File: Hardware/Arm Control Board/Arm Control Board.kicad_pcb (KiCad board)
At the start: 2 copper layers, 112 parts, among them P1 Servo 1, P10 UIM240XX_Stepper_Conn, P11 Battery, P12 SyRen, P13 Raspberry Pi, P14 Gripper Force Fdbk, P2 Shoulder Feedback, P3 Servo 2, P4 Servo 3, P5 Elbow Feedback, P6 Servo 4, P7 RS485, P8 ST_SWD_Connector, P9 Servo 5, U1 STM32F401RCT6, U10 ZXCT1107, U11 ZXCT1107, U12 ZXCT1107, U13 ZXCT1107, U2 SN75176BDR, U3 74LVCH244APW, U4 AOZ1280CI, U5 AOZ1280CI, U6 AP65552SP-13, U7 AP65552SP-13, U8 AP65552SP-13, U9 AP65552SP-13, X1 24MHz

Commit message: Connecting more things in better ways
Just in case i screw something up
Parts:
- moved P13 130.7 mm to (161.2, 101.8), turned to 0 degrees
- moved P7 127.0 mm to (185.8, 114.2), turned to 0 degrees
- moved U2 121.4 mm to (192.4, 114.2)
- moved P12 116.0 mm to (195.2, 100.4), turned to 90 degrees
- moved C1 112.9 mm to (192.2, 110.0)
- moved C51 106.9 mm to (215.4, 100.6)
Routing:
- net /Servo1_PWM: track 0.00 -> 113.4 mm, vias 0 -> 6
- net /7.4V Regulators/REG1EN: track 0.01 -> 107.4 mm, vias 0 -> 4
- net /7.4V Regulators/REG4CURRENT: track 4.01 -> 85.2 mm, vias 0 -> 4
- net /7.4V Regulators/REG1CURRENT: track 3.27 -> 77.3 mm
- net /Servo5_PWM: track 0.00 -> 68.6 mm, vias 0 -> 2
- net /Low Voltage Regulators/REG5+5V: track 0.00 -> 62.5 mm, vias 0 -> 4
- net /Low Voltage Regulators/REG5EN: track 0.22 -> 61.1 mm, vias 0 -> 4
- net /7.4V Regulators/REG4EN: track 0.99 -> 55.5 mm, vias 0 -> 2
- net /Servo4_PWM: track 0.00 -> 50.1 mm, vias 0 -> 2
- net /Servo3_PWM: track 0.00 -> 25.0 mm
- net /USART1_RX: track 0.00 -> 17.8 mm, vias 0 -> 2
- net Net-(C51-Pad1): track 1.13 -> 14.1 mm, vias 0 -> 2
- net /USART1_TX: track 0.00 -> 12.6 mm
- net Net-(U1-Pad41): track 1.27 -> 13.2 mm
- net /485_B: track 11.5 -> 3.08 mm
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
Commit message: Connect everything but 12V and GND
Not like those lines are really necessary. MAVRIC is more than capable
of running off of team spirit, optimism, and enthusiasm.
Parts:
- moved P11 142.5 mm to (156.0, 116.0), turned to 90 degrees
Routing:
- net /7.4V Regulators/REG3CURRENT: track 2.77 -> 177.2 mm, vias 0 -> 8
- net /7.4V Regulators/REG2EN: track 0.00 -> 130.2 mm, vias 0 -> 4
- net /7.4V Regulators/REG2CURRENT: track 3.08 -> 105.8 mm, vias 0 -> 2
- net /Low Voltage Regulators/REG6EN: track 0.47 -> 99.1 mm, vias 0 -> 2
- net /Servo2_PWM: track 0.00 -> 96.5 mm, vias 0 -> 4
- net /ADC1_IN9_Elbow: track 0.00 -> 95.0 mm, vias 0 -> 4
- net /ADC1_IN8_Shoulder: track 0.21 -> 89.9 mm, vias 0 -> 4
- net /ADC1_IN10_GripForce: track 0.00 -> 63.5 mm, vias 0 -> 4
- net /7.4V Regulators/REG3EN: track 0.49 -> 55.5 mm, vias 0 -> 8
- net /Low Voltage Regulators/REG6+3V3: track 91.7 -> 145.2 mm, vias 0 -> 4
- net /Step_Step: track 0.00 -> 21.7 mm, vias 0 -> 2
- net /Low Voltage Regulators/REG5+5V: track 62.5 -> 75.7 mm
- net /Low Voltage Regulators/REG5EN: track 61.1 -> 72.0 mm
- net /Step_Enable: track 20.2 -> 18.5 mm
- net /Servo1_PWM: track 113.4 -> 114.7 mm
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
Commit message: Condensing Stage 1
Just an intermediate commit in case something goes horribly wrong
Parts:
- moved C35 16.3 mm to (221.2, 143.8)
- moved C37 16.3 mm to (226.2, 143.0)
- moved C39 16.3 mm to (231.2, 140.8)
- moved C41 16.3 mm to (230.4, 135.5)
- moved C43 16.3 mm to (220.9, 135.0)
- moved C44 16.3 mm to (233.2, 135.5)
- moved C47 16.3 mm to (224.4, 127.5)
- moved C49 16.3 mm to (218.2, 135.0)
- moved L5 16.3 mm to (230.2, 127.5)
- moved P4 16.3 mm to (229.3, 115.2)
- moved R11 16.3 mm to (221.2, 146.5)
- moved R13 16.3 mm to (221.2, 141.0)
- moved R15 16.3 mm to (215.4, 135.0)
- moved R21 16.3 mm to (229.3, 120.2)
- moved R23 16.3 mm to (235.1, 114.9)
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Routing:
- net /7.4V Regulators/REG3CURRENT: track 177.2 -> 130.0 mm, vias 8 -> 10
- net /Servo3_PWM: track 25.0 -> 8.26 mm
- net /Servo2_PWM: track 96.5 -> 85.5 mm
- net /Servo1_PWM: track 114.7 -> 104.6 mm
- net /7.4V Regulators/REG3EN: track 55.5 -> 46.3 mm
- net /ADC1_IN10_GripForce: track 63.5 -> 56.5 mm
- net /ADC1_IN8_Shoulder: track 89.9 -> 85.5 mm
- net /Servo4_PWM: track 50.9 -> 47.1 mm
- net Net-(C22-Pad1): track 0.00 -> 3.14 mm
- net /Low Voltage Regulators/REG6EN: track 99.1 -> 101.5 mm
- net /Low Voltage Regulators/REG6+3V3: track 145.2 -> 144.1 mm
- net /7.4V Regulators/REG2CURRENT: track 105.8 -> 106.4 mm

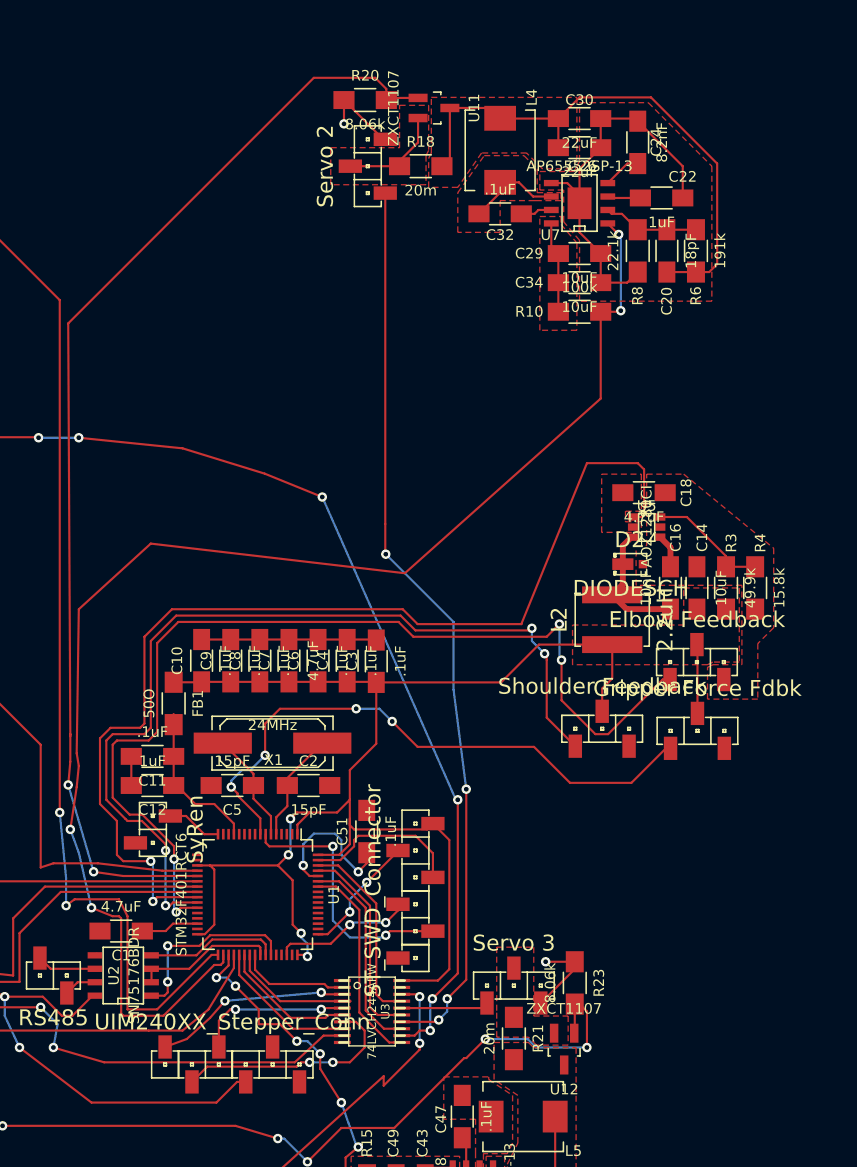
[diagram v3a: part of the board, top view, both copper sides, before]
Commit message: Condensing Stage 2
Still in progress, many of the traces are now in reasonable, space
conservative spots
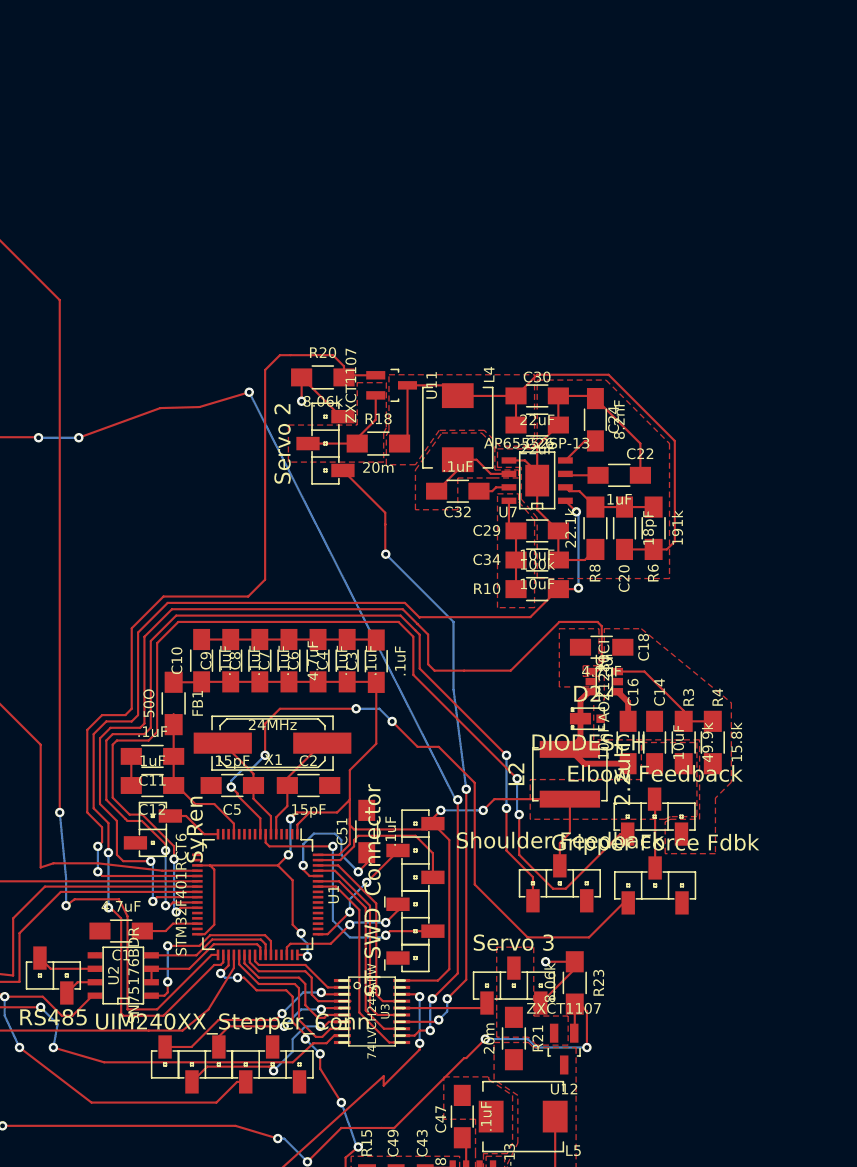
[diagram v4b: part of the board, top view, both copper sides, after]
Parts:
- moved C20 26.5 mm to (239.8, 72.0)
- moved C22 26.5 mm to (239.2, 67.0)
- moved C24 26.5 mm to (237.0, 61.7)
- moved C26 26.5 mm to (231.5, 62.2)
- moved C29 26.5 mm to (231.5, 72.2)
- moved C30 26.5 mm to (231.5, 59.5)
- moved C32 26.5 mm to (224.0, 68.5)
- moved C34 26.5 mm to (231.5, 75.0)
- moved L4 26.5 mm to (224.0, 62.5)
- moved P3 26.5 mm to (211.5, 64.0)
- moved R10 26.5 mm to (231.5, 77.7)
- moved R18 26.5 mm to (216.5, 64.0)
- moved R20 26.5 mm to (211.2, 57.7)
- moved R6 26.5 mm to (242.5, 72.0)
- moved R8 26.5 mm to (237.0, 72.0)
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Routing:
- net /Servo2_PWM: track 85.5 -> 61.0 mm
- net /7.4V Regulators/REG2EN: track 130.2 -> 106.1 mm
- net /7.4V Regulators/REG2CURRENT: track 106.4 -> 83.2 mm
- net /Low Voltage Regulators/REG6+3V3: track 144.1 -> 134.6 mm, vias 4 -> 6
- net /Low Voltage Regulators/REG6EN: track 101.5 -> 92.2 mm
- net /ADC1_IN10_GripForce: track 56.5 -> 64.2 mm
- net /ADC1_IN8_Shoulder: track 85.5 -> 91.7 mm
- net /Servo1_PWM: track 104.6 -> 109.5 mm
- net /Step_Step: track 21.7 -> 17.6 mm
- net /ADC1_IN9_Elbow: track 95.2 -> 98.3 mm
- net /TIM3_CH1_EE: track 13.8 -> 15.6 mm
- net /Step_Direction: track 14.6 -> 13.8 mm
- net /TIM3_CH2_EE: track 12.8 -> 13.5 mm

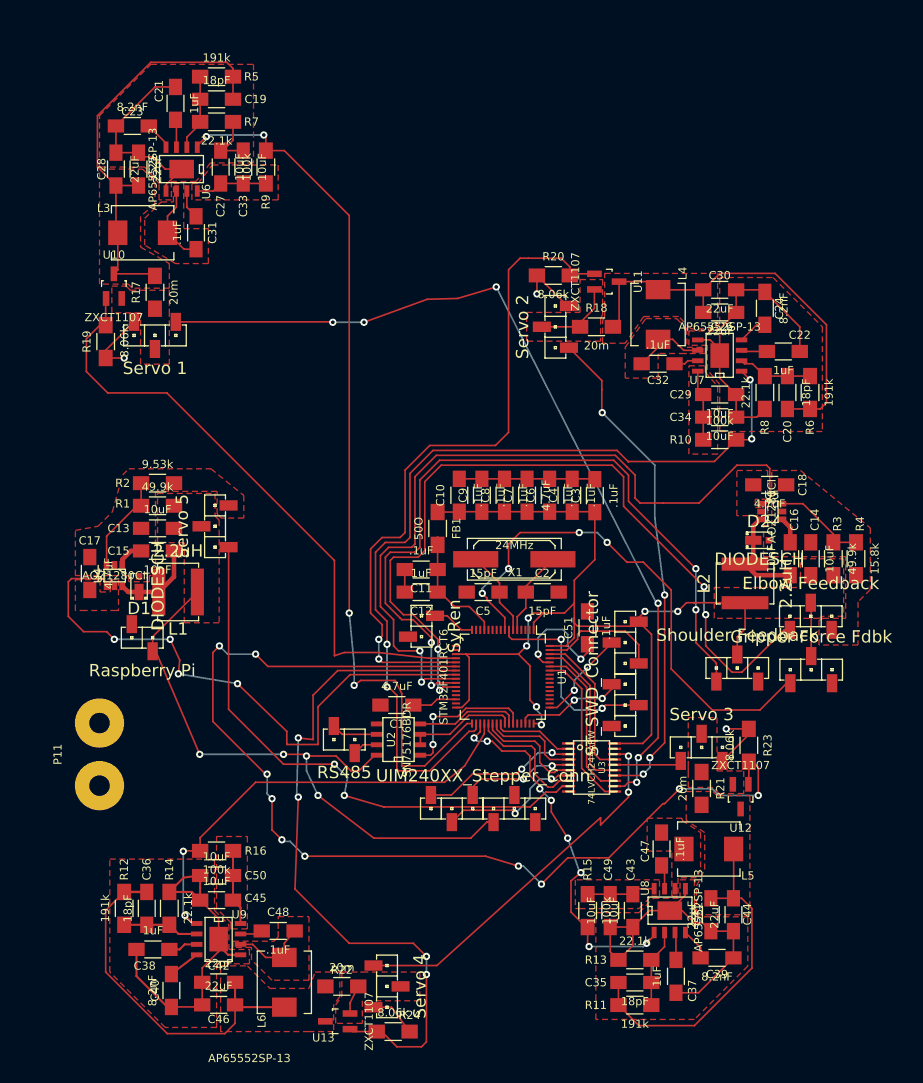
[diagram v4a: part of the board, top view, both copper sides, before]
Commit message: Condensing Stage 3 + Board Outline
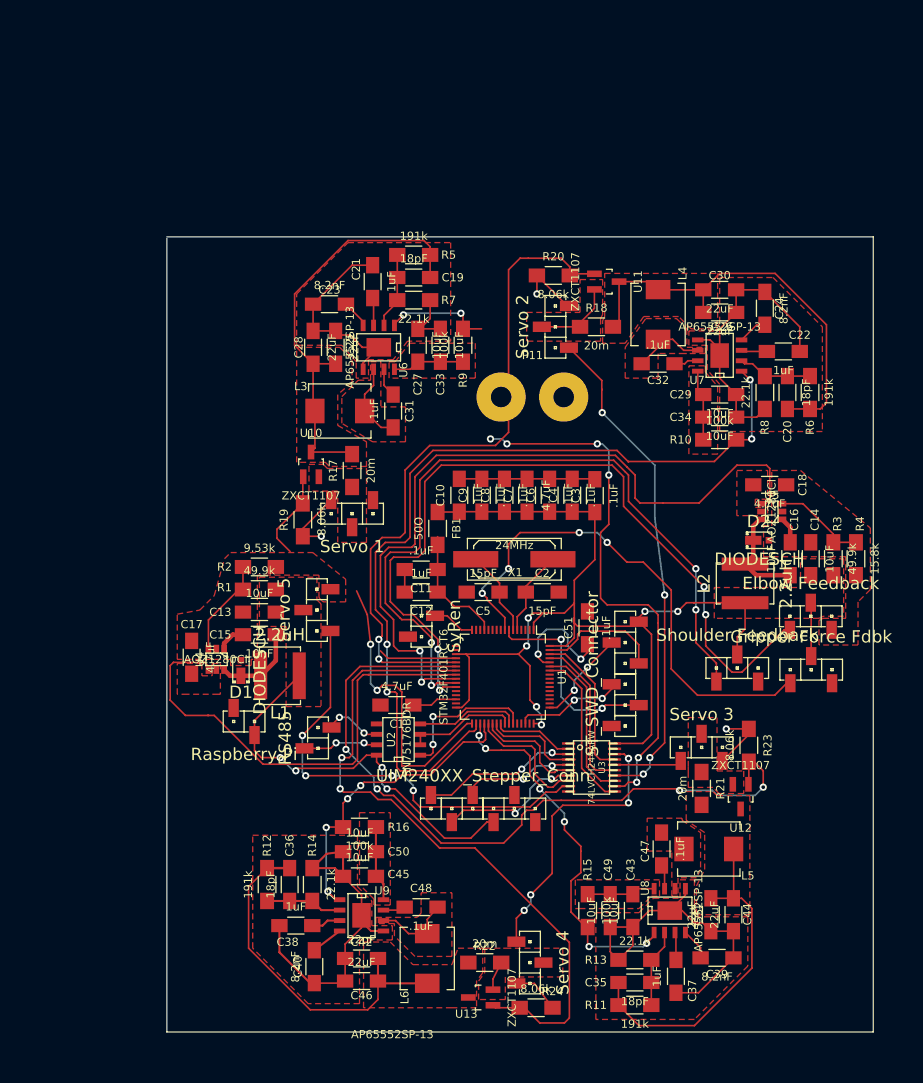
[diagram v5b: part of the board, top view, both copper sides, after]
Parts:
- moved P11 68.3 mm to (208.7, 72.5), turned to 0 degrees
- moved C19 32.4 mm to (194.2, 58.0)
- moved C21 32.4 mm to (189.2, 58.5)
- moved C23 32.4 mm to (184.0, 61.2)
- moved C25 32.4 mm to (184.8, 66.5)
- moved C27 32.4 mm to (194.8, 66.2)
- moved C28 32.4 mm to (182.0, 66.5)
- moved C31 32.4 mm to (191.8, 74.2)
- moved C33 32.4 mm to (197.5, 66.2)
- moved L3 32.4 mm to (185.2, 74.2)
- moved P1 32.4 mm to (186.8, 86.7)
- moved R17 32.4 mm to (186.8, 81.5)
- moved R19 32.4 mm to (180.8, 87.5)
- moved R5 32.4 mm to (194.2, 55.2)
- moved R7 32.4 mm to (194.2, 60.7)
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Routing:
- net /7.4V Regulators/REG1EN: track 108.0 -> 49.1 mm
- net /7.4V Regulators/REG1CURRENT: track 76.5 -> 21.4 mm
- net /Servo1_PWM: track 109.5 -> 65.6 mm
- net /7.4V Regulators/REG3CURRENT: track 130.0 -> 90.2 mm, vias 10 -> 4
- net /Low Voltage Regulators/REG5+5V: track 75.7 -> 49.2 mm
- net /7.4V Regulators/REG4EN: track 55.9 -> 38.3 mm, vias 2 -> 4
- net /Low Voltage Regulators/REG5EN: track 72.0 -> 58.2 mm, vias 4 -> 0
- net /Servo5_PWM: track 68.4 -> 54.9 mm, vias 2 -> 4
- net /Servo4_PWM: track 47.1 -> 34.4 mm, vias 2 -> 4
- net /485_B: track 3.08 -> 9.16 mm, vias 0 -> 2
- net /7.4V Regulators/REG4CURRENT: track 85.2 -> 83.4 mm, vias 4 -> 2
- net /ADC1_IN10_GripForce: track 64.2 -> 62.7 mm
- net /485_A: track 5.62 -> 7.01 mm, vias 0 -> 2
- net /7.4V Regulators/REG3EN: track 46.3 -> 45.9 mm, vias 8 -> 6
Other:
- board outline added: 239.7 x 139.3 mm

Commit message: Complete Layout Revision 1
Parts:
- moved P11 2.92 mm to (211.2, 74.0), turned to 180 degrees
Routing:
- net +12V: track 34.9 -> 218.4 mm, vias 0 -> 6
- net GND: track 220.6 -> 294.2 mm, vias 3 -> 30
- net /7.4V Regulators/REG1EN: track 49.1 -> 87.4 mm, vias 4 -> 8
- net /Servo1_PWM: track 65.6 -> 83.4 mm
- net /7.4V Regulators/REG1CURRENT: track 21.4 -> 39.1 mm
- net /Low Voltage Regulators/REG6EN: track 92.2 -> 87.5 mm, vias 2 -> 4
- net /Low Voltage Regulators/REG5EN: track 58.2 -> 60.0 mm, vias 0 -> 2
- net /Servo2_PWM: track 61.0 -> 62.7 mm, vias 4 -> 6
- net /7.4V Regulators/REG2CURRENT: track 83.2 -> 81.7 mm, vias 2 -> 4
- net /Servo4_PWM: track 34.4 -> 35.3 mm
- net /7.4V Regulators/REG3EN: track 45.9 -> 46.5 mm, vias 6 -> 8
- net /7.4V Regulators/REG2EN: vias 4 -> 6
- net (no net): vias 0 -> 1
- added copper zone on B.Cu, net GND
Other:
- outline, holes or cut-outs redrawn

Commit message: Fix board outline and export gerbers
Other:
- board size 239.7 x 139.3 mm -> 86.4 x 97.2 mm

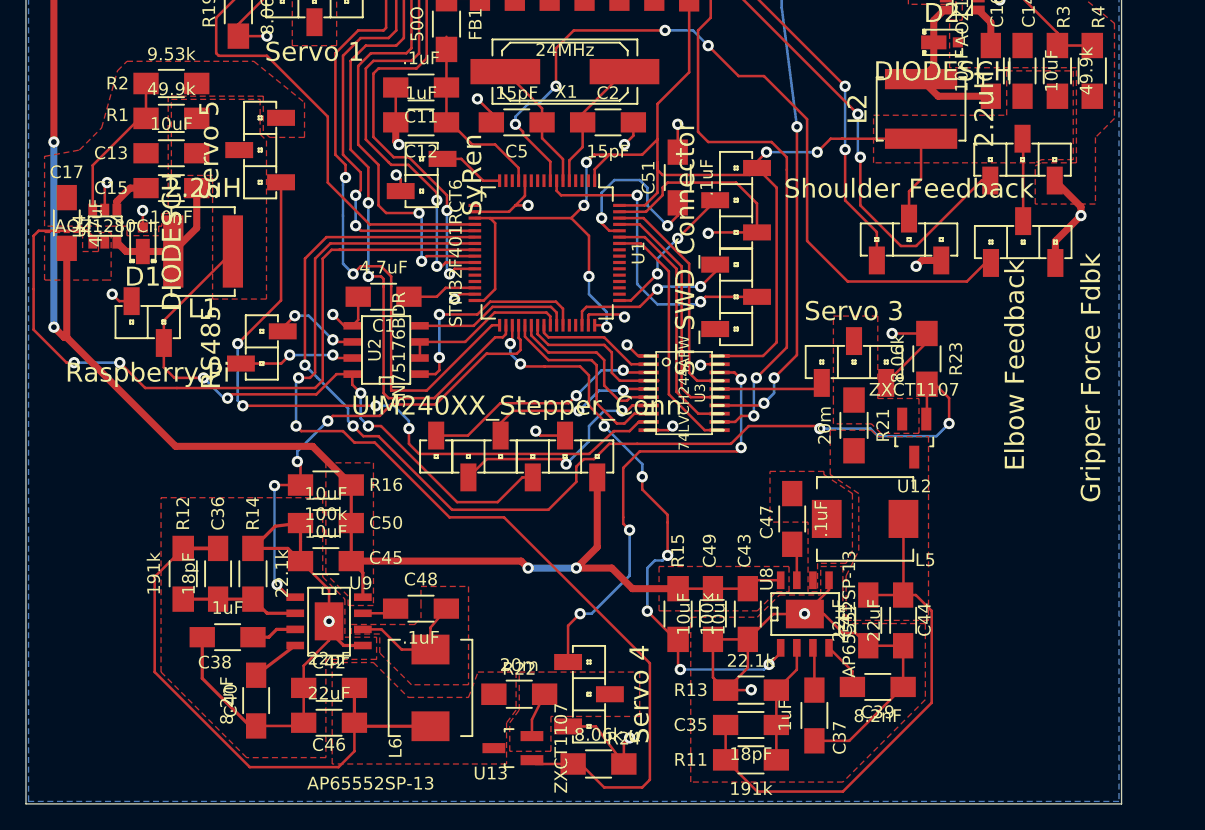
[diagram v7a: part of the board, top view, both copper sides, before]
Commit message: Improved serial and servo connectors, moved refs
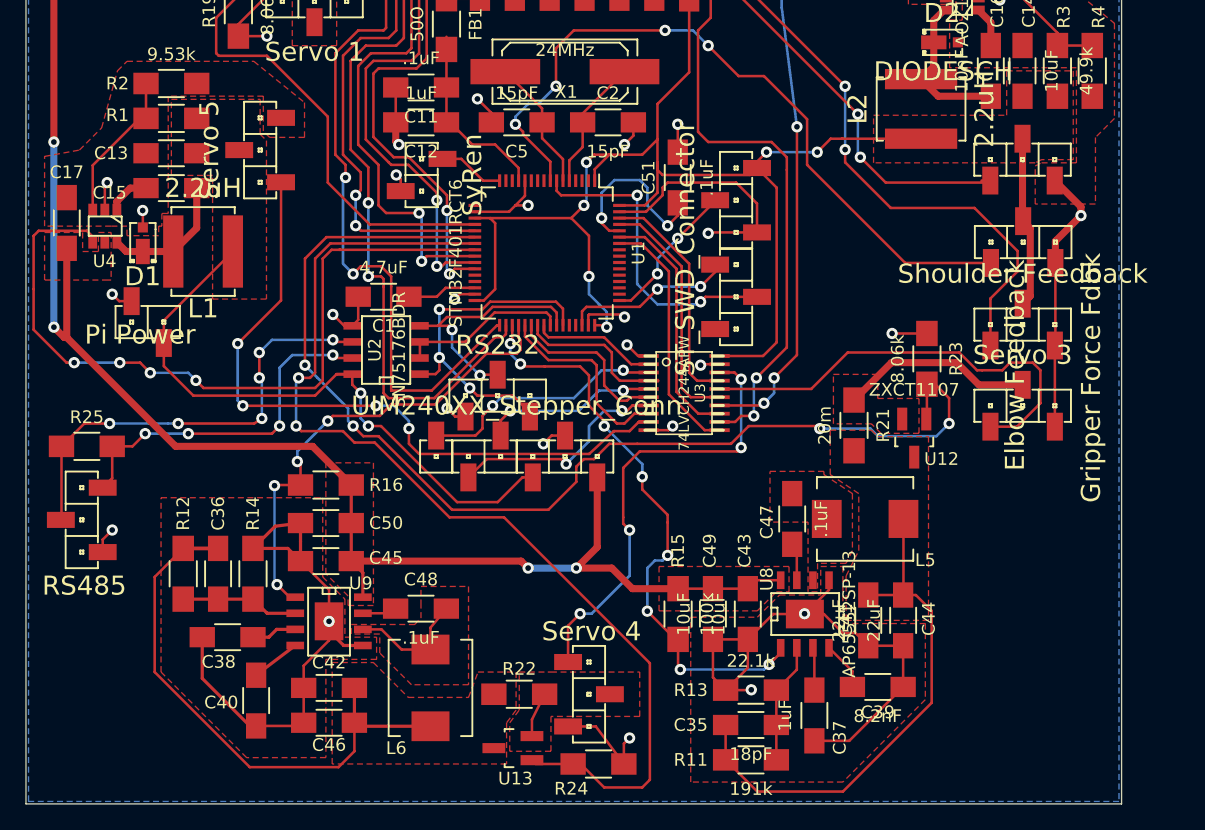
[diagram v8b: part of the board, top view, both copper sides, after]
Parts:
- added P15: RS232, MAVRIC_footprints:1x3_SMD_header, F.Cu at (201.2, 117.8)
- added R25: 100, Resistors_SMD:R_1206_HandSoldering, F.Cu at (168.8, 121.8)
- P13: value Raspberry Pi -> Pi Power
- P7: footprint MAVRIC_footprints:1x2_SMD_header -> MAVRIC_footprints:1x3_SMD_header
- moved P7 19.7 mm to (168.4, 127.6)
- moved P4 13.7 mm to (242.6, 118.6)
- moved P2 11.2 mm to (242.6, 112.2)
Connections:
- P7 pad 1: /485_A -> /485_B
- P7 pad 2: /485_B -> /485_A
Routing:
- net /485_A: track 7.01 -> 35.6 mm, vias 2 -> 6
- net /Servo3_PWM: track 8.26 -> 35.5 mm
- net /485_B: track 9.16 -> 28.3 mm, vias 2 -> 4
- net /ADC1_IN8_Shoulder: track 91.7 -> 107.7 mm
- net /7.4V Regulators/REG3+7V4: track 0.00 -> 15.2 mm
- net GND: track 294.2 -> 303.7 mm, vias 30 -> 31
- net /USART1_RX: track 17.8 -> 27.2 mm, vias 2 -> 3
- net /USART1_TX: track 12.6 -> 19.7 mm, vias 0 -> 2
- net /ADC1_IN9_Elbow: track 98.3 -> 92.6 mm
- net /ADC1_IN10_GripForce: track 62.7 -> 58.4 mm
- net /Step_Direction: track 13.8 -> 14.9 mm
- net /Low Voltage Regulators/REG5+5V: track 49.2 -> 50.2 mm, vias 4 -> 2
- net /Step_Enable: track 19.0 -> 19.5 mm
- net /Low Voltage Regulators/REG5EN: vias 2 -> 4
